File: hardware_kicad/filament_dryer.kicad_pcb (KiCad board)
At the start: 2 copper layers, 94 x 130 mm, 136 parts, among them J1 USB_C_Receptacle_USB2.0, J2 H/T Ambient, J3 T Aux, J4 Peristaltic Pump, Q3 NMOS, Q4 NMOS, Q5 NMOS, Q6 NMOS, Q7 NMOS, Q8 NMOS, U1 W25Q128JVS, U2 AMS1117-3.3, U3 RP2040, U4 DS18B20Z, U5 H/T Filament, X1 12MHz Yangxing Tech X322512MS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

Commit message: schematics
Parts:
- removed C1, C10, C11, C12, C2, C3, C6, C7, C8, C9, NeoC1, NeoC10, NeoC11, NeoC12, NeoC13, NeoC14, NeoC15, NeoC16, NeoC17, NeoC18, NeoC19, NeoC2, NeoC20, NeoC21, NeoC22, NeoC23, NeoC24, NeoC25, NeoC26, NeoC27, NeoC28, NeoC3, NeoC4, NeoC5, NeoC6, NeoC7, NeoC8, NeoC9: 100n, Capacitor_SMD:C_0402_1005Metric_Pad0.74x0.62mm_HandSolder
- removed C13, C15: 10u, Capacitor_SMD:C_0603_1608Metric
- removed C17, C18: 30p, Capacitor_SMD:C_0402_1005Metric
- removed C4, C5: 1u, Capacitor_SMD:C_0402_1005Metric_Pad0.74x0.62mm_HandSolder
- removed J1: USB_C_Receptacle_USB2.0, 00_project_library:USB_C_Receptacle_Palconn_UTC16-G
- removed JP1, JP2, JP3, JP4: SolderJumper_2_Open, Jumper:SolderJumper-2_P1.3mm_Open_RoundedPad1.0x1.5mm
- removed NeoD1, NeoD10, NeoD11, NeoD12, NeoD13, NeoD14, NeoD15, NeoD16, NeoD17, NeoD18, NeoD19, NeoD2, NeoD20, NeoD21, NeoD22, NeoD23, NeoD24, NeoD25, NeoD26, NeoD27, NeoD28, NeoD3, NeoD4, NeoD5, NeoD6, NeoD7, NeoD8, NeoD9: WS2812B-2020, LED_SMD:LED_WS2812B-2020_PLCC4_2.0x2.0mm
- removed Q3, Q4, Q5, Q6, Q7, Q8: NMOS, 00_project_library:SOT-23
- removed R10: 1k, Resistor_SMD:R_0402_1005Metric_Pad0.72x0.64mm_HandSolder
- removed R16: 4k7, Resistor_SMD:R_0402_1005Metric_Pad0.72x0.64mm_HandSolder
- removed R17, R18, R21: 4K7, Resistor_SMD:R_0402_1005Metric_Pad0.72x0.64mm_HandSolder
- removed R22, R8: 470R, Resistor_SMD:R_0402_1005Metric_Pad0.72x0.64mm_HandSolder
- removed R3, R4: 5.1K, Resistor_SMD:R_0402_1005Metric_Pad0.72x0.64mm_HandSolder
- removed R5, R6: 27R, Resistor_SMD:R_0402_1005Metric_Pad0.72x0.64mm_HandSolder
- removed R9: 10K, Resistor_SMD:R_0402_1005Metric_Pad0.72x0.64mm_HandSolder
- removed SW_BOOT1: Boot, 00_project_library:SW_TS-1187A-B-A-B
- removed SW_RESET1: Reset, 00_project_library:SW_TS-1187A-B-A-B
- removed TP1: TestPoint, TestPoint:TestPoint_Pad_D2.5mm
- removed U2: AMS1117-3.3, 00_project_library:SOT-223-3_TabPin2
- removed U3: RP2040, 00_project_library_circuitstate:RP2040-QFN-56
- removed X1: 12MHz Yangxing Tech X322512MSB4SI, 00_project_library:Crystal_SMD_3225-4Pin_3.2x2.5mm
- added D4: FAN_2, 00_project_library:LED_0603_1608Metric, F.Cu at (202.3, 99.3)
- added FanQ1: NMOS, 00_project_library:SOT-23, F.Cu at (202.3, 79.9)
- added FanQ2: NMOS, 00_project_library:SOT-23, F.Cu at (202.3, 84.3)
- added PowerQ1: NMOS, 00_project_library:SOT-23, F.Cu at (202.3, 88.8)
- added PowerQ2: NMOS, 00_project_library:SOT-23, F.Cu at (202.3, 93.2)
- added PowerR1: 120, Resistor_SMD:R_1206_3216Metric, F.Cu at (203.1, 59.6)
- added PowerR10: 120, Resistor_SMD:R_1206_3216Metric, F.Cu at (208.7, 69.4)
- added PowerR11: 120, Resistor_SMD:R_1206_3216Metric, F.Cu at (208.7, 72.7)
- added PowerR12: 120, Resistor_SMD:R_1206_3216Metric, F.Cu at (208.7, 76.0)
- added PowerR13: 120, Resistor_SMD:R_1206_3216Metric, F.Cu at (214.3, 59.6)
- added PowerR14: 120, Resistor_SMD:R_1206_3216Metric, F.Cu at (214.3, 62.9)
- added PowerR15: 120, Resistor_SMD:R_1206_3216Metric, F.Cu at (214.3, 66.2)
- added PowerR16: 120, Resistor_SMD:R_1206_3216Metric, F.Cu at (214.3, 69.4)
- added PowerR17: 120, Resistor_SMD:R_1206_3216Metric, F.Cu at (214.3, 72.7)
- added PowerR18: 120, Resistor_SMD:R_1206_3216Metric, F.Cu at (214.3, 76.0)
- added PowerR19: 120, Resistor_SMD:R_1206_3216Metric, F.Cu at (219.9, 59.6)
- added PowerR2: 120, Resistor_SMD:R_1206_3216Metric, F.Cu at (203.1, 62.9)
- added PowerR20: 120, Resistor_SMD:R_1206_3216Metric, F.Cu at (219.9, 62.9)
- added PowerR21: 120, Resistor_SMD:R_1206_3216Metric, F.Cu at (219.9, 66.2)
- added PowerR22: 120, Resistor_SMD:R_1206_3216Metric, F.Cu at (219.9, 69.4)
- added PowerR23: 120, Resistor_SMD:R_1206_3216Metric, F.Cu at (219.9, 72.7)
- added PowerR24: 120, Resistor_SMD:R_1206_3216Metric, F.Cu at (219.9, 76.0)
- added PowerR3: 120, Resistor_SMD:R_1206_3216Metric, F.Cu at (203.1, 66.2)
- added PowerR4: 120, Resistor_SMD:R_1206_3216Metric, F.Cu at (203.1, 69.4)
- added PowerR5: 120, Resistor_SMD:R_1206_3216Metric, F.Cu at (203.1, 72.7)
- added PowerR6: 120, Resistor_SMD:R_1206_3216Metric, F.Cu at (203.1, 76.0)
- added PowerR7: 120, Resistor_SMD:R_1206_3216Metric, F.Cu at (208.7, 59.6)
- added PowerR8: 120, Resistor_SMD:R_1206_3216Metric, F.Cu at (208.7, 62.9)
- added PowerR9: 120, Resistor_SMD:R_1206_3216Metric, F.Cu at (208.7, 66.2)
- D3: value POW_LED -> FAN_2
- R1: value 4K7 -> 470R
- R2: value 10K -> 470R
- U1: value W25Q128JVS -> Pico; footprint 00_project_library:SOIC-8_5.23x5.23mm_P1.27mm -> 00_project_library:RPi_Pico_SMD_TH
- moved D3 123.4 mm to (202.3, 96.8), turned to 0 degrees
- moved R2 122.3 mm to (201.9, 101.6), turned to 0 degrees
- moved R15 110.3 mm to (201.9, 103.6)
- moved J4 49.0 mm to (67.3, 75.7), turned to 180 degrees
- moved U5 32.6 mm to (139.5, 81.5)
- moved R14 32.6 mm to (137.8, 86.8)
- moved C20 32.6 mm to (139.5, 86.9)
- moved R13 32.6 mm to (131.3, 84.1)
- moved R12 32.6 mm to (143.5, 82.3)
- moved J3 31.2 mm to (67.4, 89.0), turned to 180 degrees
- moved U1 24.0 mm to (102.5, 85.2), turned to 90 degrees
- moved J2 15.6 mm to (67.4, 102.7), turned to 180 degrees
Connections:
- D3 pad 2: +3V3 -> +5V
- R1 pad 1: +5V -> Net-(D4-K)
- R2 pad 1: +3V3 -> Net-(D3-K)
- R2 pad 2: /QSPI_SS -> Net-(PowerQ1-D)
- U1 pad 1: /QSPI_SS -> unconnected-(U1-GPIO0-Pad1)
- U1 pad 2: /QSPI_SD1 -> unconnected-(U1-GPIO1-Pad2)
- U1 pad 3: /QSPI_SD2 -> unconnected-(U1-GND-Pad3)
- U1 pad 4: GND -> unconnected-(U1-GPIO2-Pad4)
- U1 pad 5: /QSPI_SD0 -> unconnected-(U1-GPIO3-Pad5)
- U1 pad 6: /QSPI_SCLK -> unconnected-(U1-GPIO4-Pad6)
- U1 pad 7: /QSPI_SD3 -> unconnected-(U1-GPIO5-Pad7)
- U1 pad 8: +3V3 -> unconnected-(U1-GND-Pad8)
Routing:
- net +3V3: track 424.0 -> 71.0 mm, vias 14 -> 2
- net +5V: track 295.0 -> 84.6 mm, vias 2 -> 0
- net /GPIO_FAN_AMBIENT: track 107.5 -> 0.00 mm, vias 4 -> 0
- net /HT_BOARD_SDA: track 107.3 -> 0.00 mm, vias 3 -> 0
- net /HT_BOARD_SCL: track 117.2 -> 11.4 mm, vias 4 -> 0
- net /GPIO_FAN_SILICAGEL: track 99.2 -> 0.00 mm, vias 2 -> 0
- net GND: track 189.3 -> 92.3 mm, vias 109 -> 15
- net Net-(JP2-B): track 91.1 -> 0.00 mm
- net /T_HEATING_1WIRE: track 90.4 -> 0.00 mm, vias 3 -> 0
- net Net-(PowerQ2-D): track 79.2 -> 0.00 mm
- net Net-(JP3-B): track 64.4 -> 0.00 mm
- net /RUN: track 54.6 -> 0.00 mm, vias 2 -> 0
- net /GPIO_NP_BOARD: track 48.2 -> 0.00 mm
- net /QSPI_SS: track 38.3 -> 0.00 mm
- net /GPIO_NP_B: track 35.8 -> 0.00 mm, vias 2 -> 0
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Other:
- board text removed: "*"
- board text removed: "RP2040"

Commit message: 20230917p_filament_dryer_silicagel.FCStd
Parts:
- removed dryer_print3D1: dryer_print3D, 00_project_library:dryer_print3d
- added REF**: dryer_print3d, 00_project_library:dryer_print3d, F.Cu at (101.0, 170.0)
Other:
- board size 94 x 130 mm -> 94 x 146.7 mm

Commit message: schematics ready for review
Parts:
- removed J2: H/T Ambient, 00_project_library:grove_vert_holes
- removed J3: T Aux, 00_project_library:grove_vert_holes
- removed R13, R14: 10k, Resistor_SMD:R_0402_1005Metric_Pad0.72x0.64mm_HandSolder
- removed REF**: dryer_print3d, 00_project_library:dryer_print3d
- added C1: 10u, Capacitor_SMD:C_0603_1608Metric, F.Cu at (16.2, 51.4)
- added C2: 10u, Capacitor_SMD:C_0603_1608Metric, F.Cu at (16.2, 53.9)
- added R22: 470R, Resistor_SMD:R_0402_1005Metric_Pad0.72x0.64mm_HandSolder, F.Cu at (15.8, 43.5)
- added R3: 10k, Resistor_SMD:R_0402_1005Metric_Pad0.72x0.64mm_HandSolder, F.Cu at (15.8, 29.6)
- added R4: 10k, Resistor_SMD:R_0402_1005Metric_Pad0.72x0.64mm_HandSolder, F.Cu at (15.8, 31.6)
- added R5: 10k, Resistor_SMD:R_0402_1005Metric_Pad0.72x0.64mm_HandSolder, F.Cu at (15.8, 33.6)
- added R6: 10k, Resistor_SMD:R_0402_1005Metric_Pad0.72x0.64mm_HandSolder, F.Cu at (15.8, 35.6)
- added R7: 10k, Resistor_SMD:R_0402_1005Metric_Pad0.72x0.64mm_HandSolder, F.Cu at (15.8, 37.5)
- added R8: 10k, Resistor_SMD:R_0402_1005Metric_Pad0.72x0.64mm_HandSolder, F.Cu at (15.8, 39.5)
- added U2: H/T Filament, 00_project_library:SON50P250X250X90-9T110X180N, F.Cu at (16.0, 47.3)
- added U3: H/T Filament, 00_project_library:SON50P250X250X90-9T110X180N, F.Cu at (19.6, 47.3)
- added dryer_print3D1: dryer_print3D, 00_project_library:dryer_print3d, F.Cu at (101.0, 170.0)
- D3: value FAN_2 -> Power_LED_1
- D4: value FAN_2 -> Power_LED_2
- H1, H2, H3, H4, H5: footprint MountingHole:MountingHole_3.2mm_M3 -> 00_project_library:MountingHole_3.2mm_M3
- R15: value 4k7 -> 2k
- TP11: value HT_SILICAGEL_SCL -> HT_AMBIENT_SCL
- TP2: value HT_SILICAGEL_GND -> HT_AMBIENT_GND
- TP3: value HT_SILICAGEL_3V3 -> HT_AMBIENT_3V3
- TP6: value HT_SILICAGEL_SCA -> HT_AMBIENT_SCA
- U5: value H/T Filament -> H/T Silicagel
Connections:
- PowerQ1 pad 2: /GPIO_HEATER -> /GPIO_HEATER_A
- PowerQ2 pad 2: /GPIO_HEATER -> /GPIO_HEATER_B
- R12 pad 1: +3V3 -> Net-(U5-~{RESET})
- R12 pad 2: Net-(U5-~{RESET}) -> GND
- TP11 pad 1: /HT_BOARD_SCL -> /HT_AMBIENT_SCL
- TP6 pad 1: /HT_BOARD_SDA -> /HT_AMBIENT_SDA
- U5 pad 1: /HT_BOARD_SDA -> /HT_FILAMENT_SDA
- U5 pad 4: /HT_BOARD_SCL -> /HT_FILAMENT_SCL
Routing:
- net /HT_FILAMENT_SCL: track 0.00 -> 11.4 mm
- net /HT_BOARD_SCL: track 11.4 -> 0.00 mm
- net GND: track 92.3 -> 91.7 mm

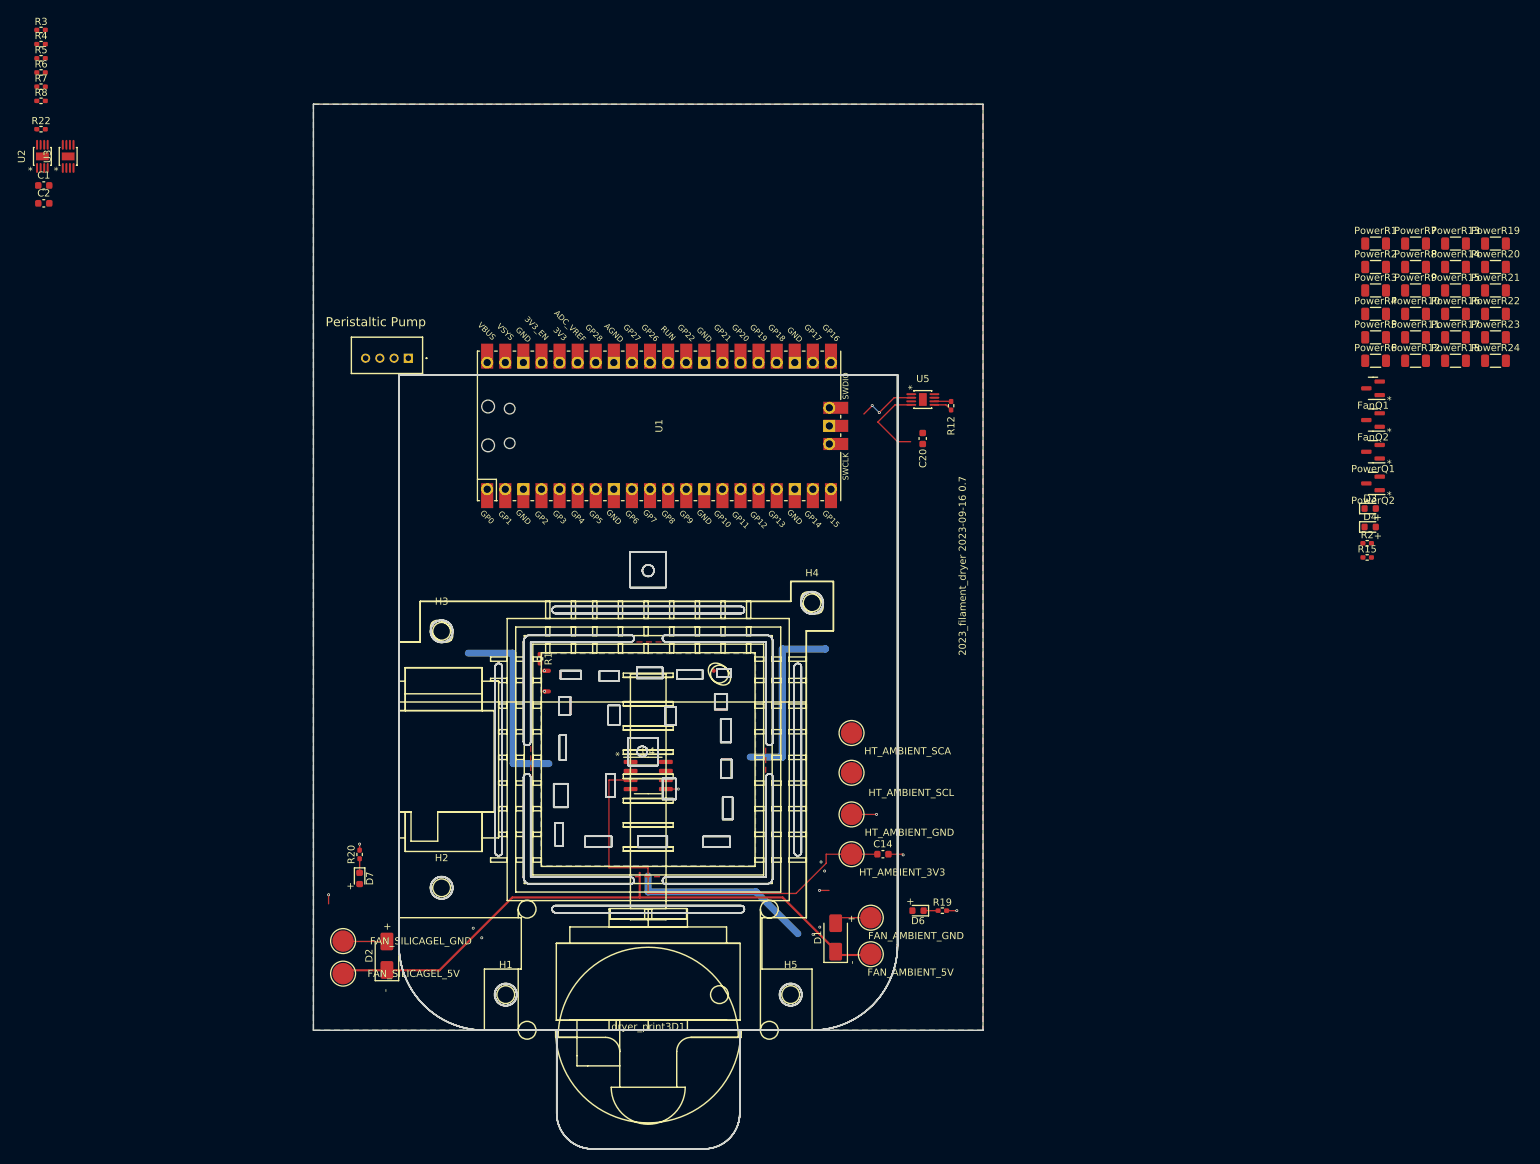
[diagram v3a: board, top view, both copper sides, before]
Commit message: board outline cleaned up
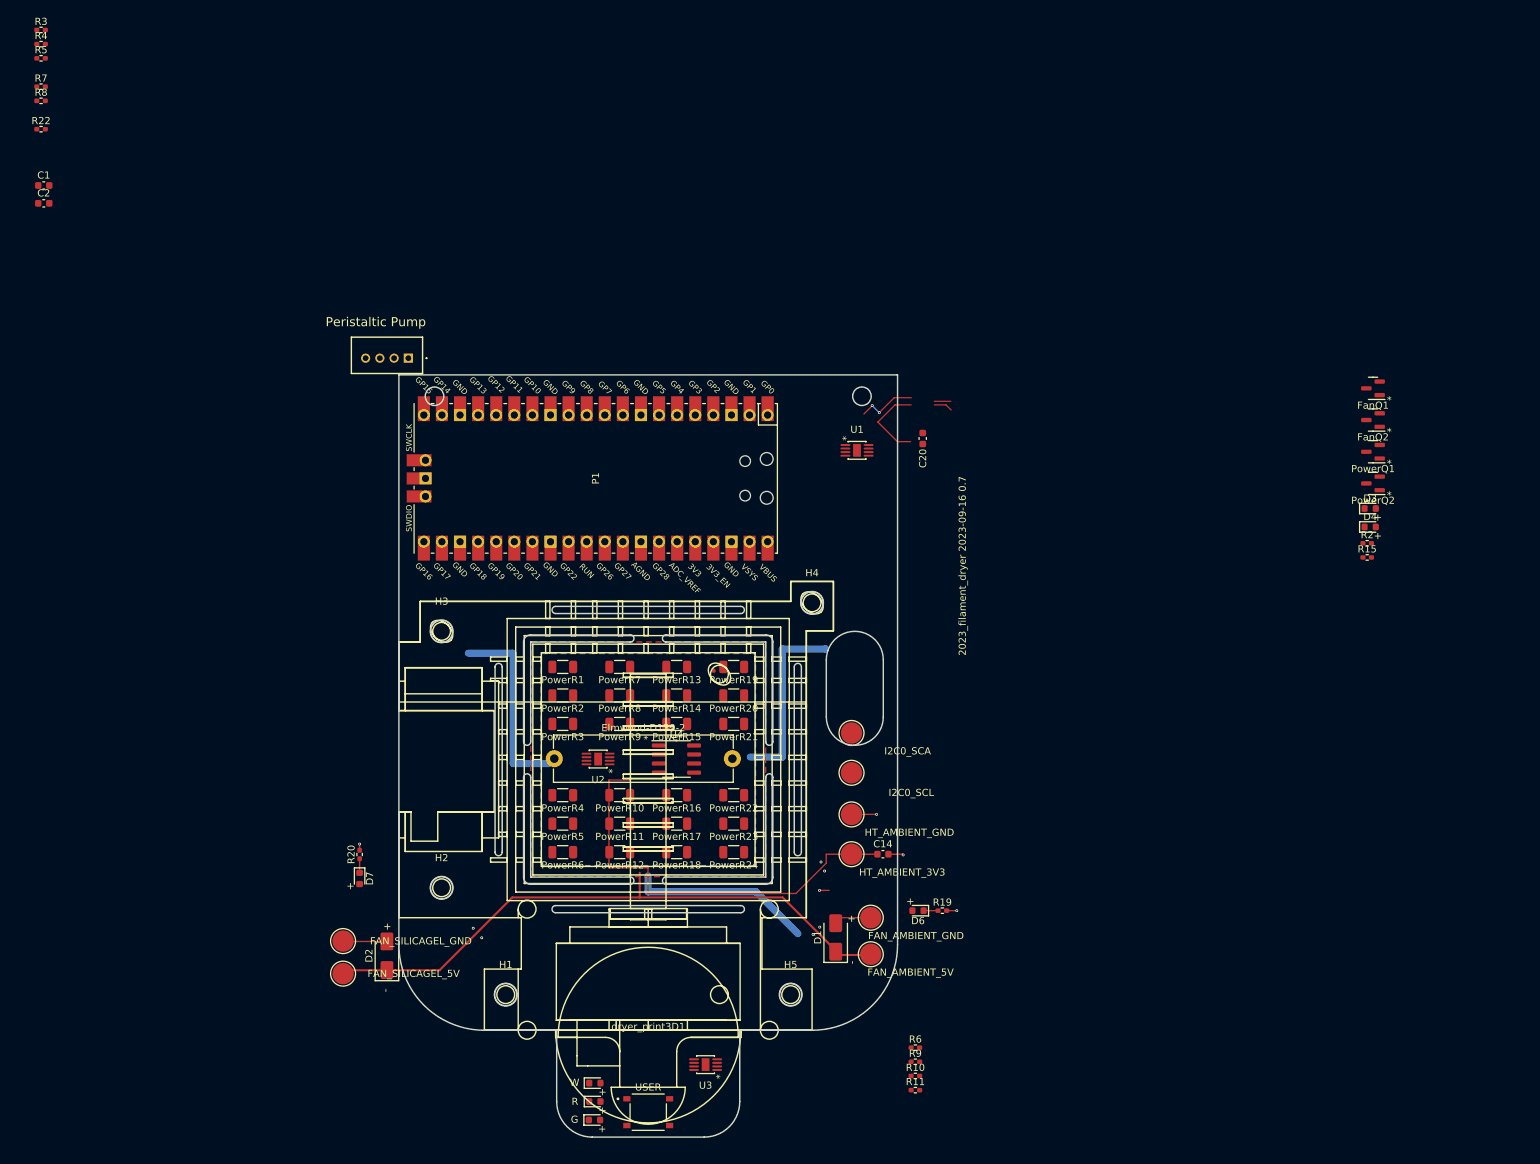
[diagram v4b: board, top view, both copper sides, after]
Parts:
- removed R1: 470R, Resistor_SMD:R_0402_1005Metric_Pad0.72x0.64mm_HandSolder
- removed R12: 10k, Resistor_SMD:R_0402_1005Metric_Pad0.72x0.64mm_HandSolder
- removed U5: H/T Silicagel, 00_project_library:SON50P250X250X90-9T110X180N
- added D5: W, 00_project_library:LED_0603_1608Metric, F.Cu at (93.5, 177.4)
- added D8: R, 00_project_library:LED_0603_1608Metric, F.Cu at (93.5, 180.0)
- added D9: G, 00_project_library:LED_0603_1608Metric, F.Cu at (93.5, 182.6)
- added Elmwood-D139-2: Thermal Fulse, 00_project_library:Thermal Fuse (R_Axial_Power_L25.0mm_W6.4mm_P27.94mm), F.Cu at (87.8, 131.9)
- added P1: Pico, 00_project_library:RPi_Pico_SMD_TH, F.Cu at (93.6, 92.5)
- added R10: 470R, Resistor_SMD:R_0402_1005Metric_Pad0.72x0.64mm_HandSolder, F.Cu at (138.5, 176.4)
- added R11: 470R, Resistor_SMD:R_0402_1005Metric_Pad0.72x0.64mm_HandSolder, F.Cu at (138.5, 178.4)
- added R9: 470R, Resistor_SMD:R_0402_1005Metric_Pad0.72x0.64mm_HandSolder, F.Cu at (138.5, 174.4)
- added USER_BUTTON1: USER, 00_project_library:SW_TS-1187A-B-A-B, F.Cu at (101.0, 181.5)
- R15: value 2k -> 4k7
- R3: value 10k -> 470R
- R6: value 10k -> 10K
- TP11: value HT_AMBIENT_SCL -> I2C0_SCL
- TP6: value HT_AMBIENT_SCA -> I2C0_SCA
- U1: value Pico -> H/T Filament; footprint 00_project_library:RPi_Pico_SMD_TH -> 00_project_library:SON50P250X250X90-9T110X180N
- U2: value H/T Filament -> H/T Silicagel
- U3: value H/T Filament -> H/T Ambient
- moved R6 183.8 mm to (138.5, 172.4)
- moved U3 155.8 mm to (109.1, 174.8), turned to 90 degrees
- moved PowerR6 133.3 mm to (89.0, 145.0), turned to 180 degrees
- moved PowerR5 133.0 mm to (89.0, 141.0), turned to 180 degrees
- moved PowerR4 132.6 mm to (89.0, 137.0), turned to 180 degrees
- moved PowerR12 131.3 mm to (97.0, 145.0), turned to 180 degrees
- moved PowerR11 130.9 mm to (97.0, 141.0), turned to 180 degrees
- moved PowerR10 130.6 mm to (97.0, 137.0), turned to 180 degrees
- moved PowerR3 129.3 mm to (89.0, 127.0), turned to 180 degrees
- moved PowerR18 129.3 mm to (105.0, 145.0), turned to 180 degrees
- moved PowerR2 129.0 mm to (89.0, 123.0), turned to 180 degrees
- moved PowerR17 128.9 mm to (105.0, 141.0), turned to 180 degrees
- moved PowerR1 128.7 mm to (89.0, 119.0), turned to 180 degrees
- moved PowerR16 128.5 mm to (105.0, 137.0), turned to 180 degrees
- moved PowerR24 127.3 mm to (113.0, 145.0), turned to 180 degrees
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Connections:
- J4 pad 2: unconnected-(J4-Pad2) -> Net-(J4-Pad2)
- PowerR1 pad 1: +5V -> Net-(Elmwood-D139-2-Pad2)
- PowerR10 pad 1: +5V -> Net-(Elmwood-D139-2-Pad2)
- PowerR11 pad 1: +5V -> Net-(Elmwood-D139-2-Pad2)
- PowerR12 pad 1: +5V -> Net-(Elmwood-D139-2-Pad2)
- PowerR13 pad 1: +5V -> Net-(Elmwood-D139-2-Pad2)
- PowerR14 pad 1: +5V -> Net-(Elmwood-D139-2-Pad2)
- PowerR15 pad 1: +5V -> Net-(Elmwood-D139-2-Pad2)
- PowerR16 pad 1: +5V -> Net-(Elmwood-D139-2-Pad2)
- PowerR17 pad 1: +5V -> Net-(Elmwood-D139-2-Pad2)
- PowerR18 pad 1: +5V -> Net-(Elmwood-D139-2-Pad2)
- PowerR19 pad 1: +5V -> Net-(Elmwood-D139-2-Pad2)
- PowerR2 pad 1: +5V -> Net-(Elmwood-D139-2-Pad2)
- PowerR20 pad 1: +5V -> Net-(Elmwood-D139-2-Pad2)
- PowerR21 pad 1: +5V -> Net-(Elmwood-D139-2-Pad2)
- PowerR22 pad 1: +5V -> Net-(Elmwood-D139-2-Pad2)
- PowerR23 pad 1: +5V -> Net-(Elmwood-D139-2-Pad2)
- PowerR24 pad 1: +5V -> Net-(Elmwood-D139-2-Pad2)
- PowerR3 pad 1: +5V -> Net-(Elmwood-D139-2-Pad2)
- PowerR4 pad 1: +5V -> Net-(Elmwood-D139-2-Pad2)
- PowerR5 pad 1: +5V -> Net-(Elmwood-D139-2-Pad2)
- PowerR6 pad 1: +5V -> Net-(Elmwood-D139-2-Pad2)
- PowerR7 pad 1: +5V -> Net-(Elmwood-D139-2-Pad2)
- PowerR8 pad 1: +5V -> Net-(Elmwood-D139-2-Pad2)
- PowerR9 pad 1: +5V -> Net-(Elmwood-D139-2-Pad2)
- R3 pad 1: +3V3 -> /GPIO_PUMP_ENABLE
- R3 pad 2: Net-(U2-~{RESET}) -> Net-(J4-Pad2)
- R4 pad 2: /HT_FILAMENT_SDA -> /I2C1_SDA
- R5 pad 2: /HT_FILAMENT_SCL -> /I2C1_SCL
- R6 pad 2: Net-(U3-~{RESET}) -> /GPIO_USER_BUTTON
- R7 pad 2: /HT_AMBIENT_SDA -> /I2C0_SDA
- R8 pad 2: /HT_AMBIENT_SCL -> /I2C0_SCL
- U1 pad 1: unconnected-(U1-GPIO0-Pad1) -> /I2C1_SDA
- U1 pad 2: unconnected-(U1-GPIO1-Pad2) -> +3V3
- U1 pad 4: unconnected-(U1-GPIO2-Pad4) -> /I2C1_SCL
- U1 pad 5: unconnected-(U1-GPIO3-Pad5) -> +3V3
- U1 pad 7: unconnected-(U1-GPIO5-Pad7) -> GND
- U1 pad 8: unconnected-(U1-GND-Pad8) -> GND
- U1 pad 9: unconnected-(U1-GPIO6-Pad9) -> GND
- U2 pad 1: /HT_FILAMENT_SDA -> /I2C1_SDA
- U2 pad 2: +3V3 -> GND
- U2 pad 4: /HT_FILAMENT_SCL -> /I2C1_SCL
- U2 pad 6: Net-(U2-~{RESET}) -> unconnected-(U2-~{RESET}-Pad6)
- U3 pad 1: /HT_AMBIENT_SDA -> /I2C0_SDA
- U3 pad 4: /HT_AMBIENT_SCL -> /I2C0_SCL
- U3 pad 6: Net-(U3-~{RESET}) -> unconnected-(U3-~{RESET}-Pad6)
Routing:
- net GND: track 91.7 -> 63.1 mm, vias 15 -> 11
- net +5V: track 84.6 -> 111.3 mm
- net (no net): track 0.00 -> 14.1 mm
- net /HT_FILAMENT_SCL: track 11.4 -> 0.00 mm
- net +3V3: track 71.0 -> 68.3 mm
- net Net-(U5-~{RESET}): track 2.32 -> 0.00 mm
- removed copper zone on F.Cu, net GND
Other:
- board size 94 x 146.7 mm -> 70 x 107 mm
